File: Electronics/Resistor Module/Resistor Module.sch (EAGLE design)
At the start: 121 parts, among them U1 74HC595D, U2 74HC595D, U3 74HC595D, U4 74HC595D, U5 25AA010A

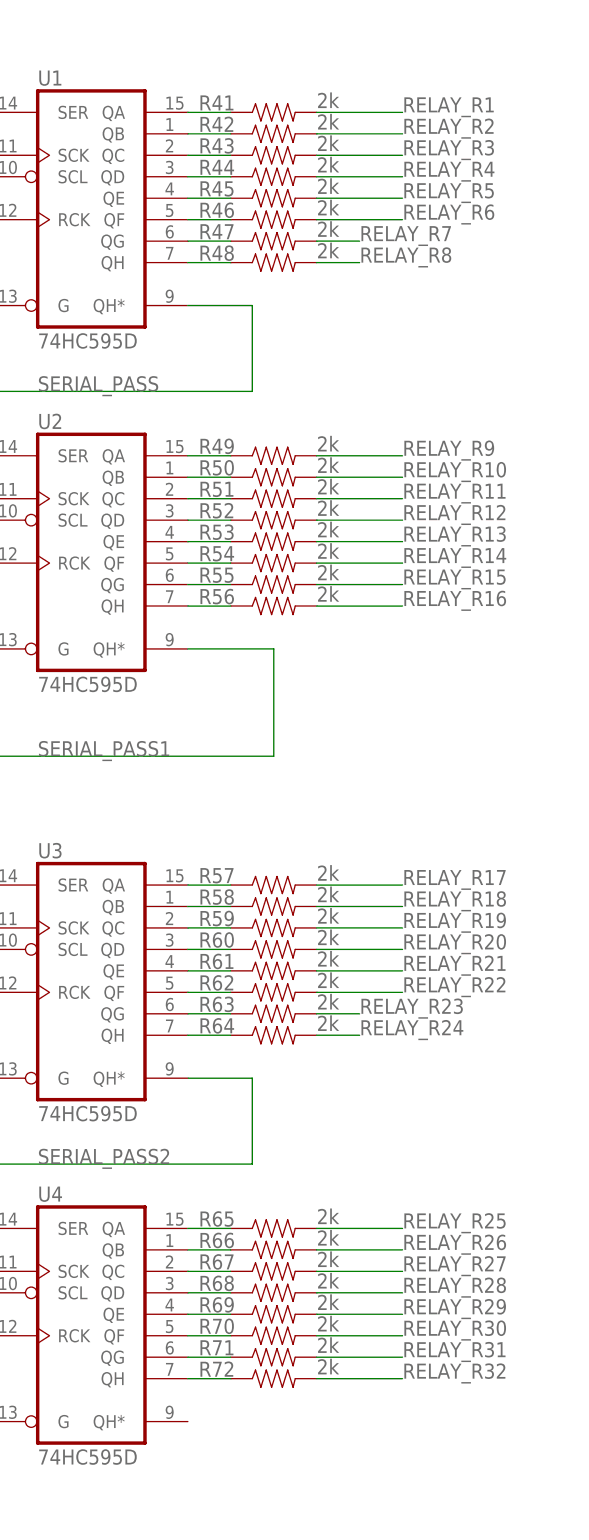
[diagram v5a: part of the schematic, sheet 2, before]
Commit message: Finished routing. Was more convenient for routing to use inverted byte order for the serial passing.
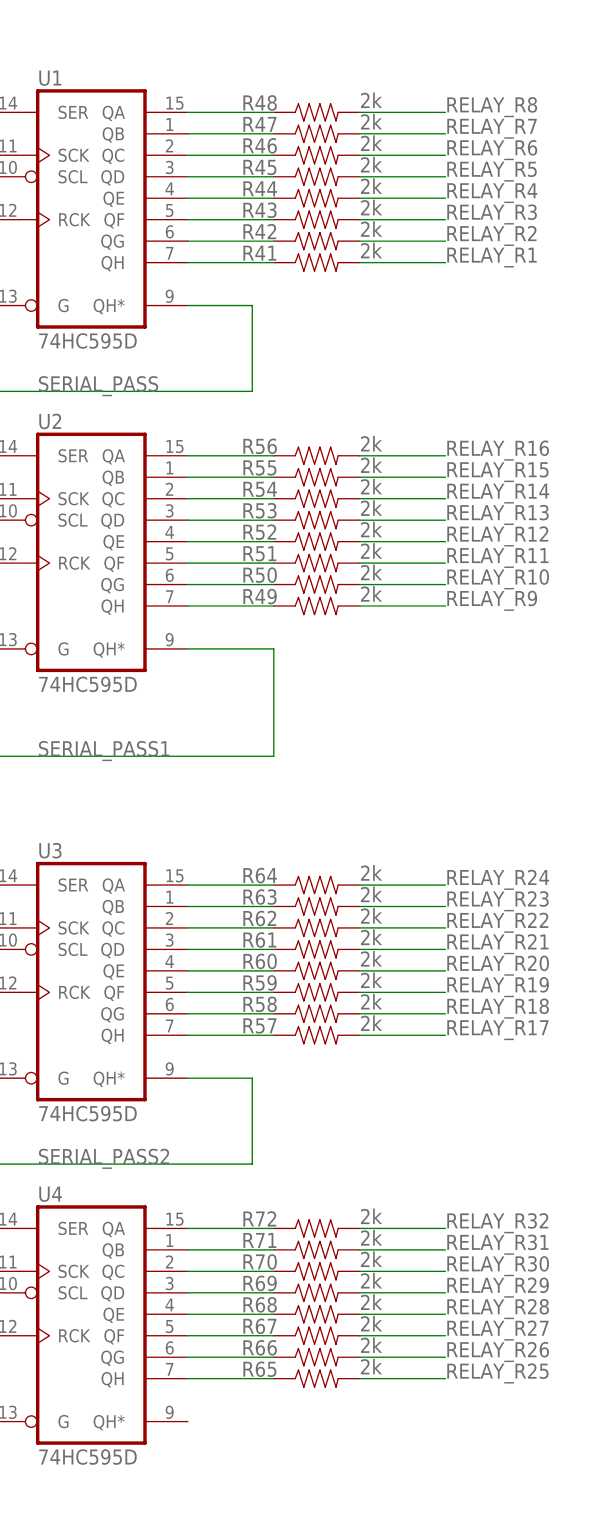
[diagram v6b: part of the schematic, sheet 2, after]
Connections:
- removed net N$61: R49.1, U2A.QA
- removed net N$62: R57.1, U3A.QA
- removed net N$64: R65.1, U4A.QA
- new net N$40: R67.1, U4A.QF
- new net N$43: R66.1, U4A.QG
- new net N$9: R46.1, U1A.QC
- net GND: no longer S17.C-, S18.C-, S19.C-, S20.C-, S21.C-, S22.C-, S23.C-, S24.C-, S25.C-, S26.C-, S27.C-, S28.C-, S29.C-, S30.C-, S31.C-, S32.C-
- net GND_2: now also S17.C-, S18.C-, S19.C-, S20.C-, S21.C-, S22.C-, S23.C-, S24.C-, S25.C-, S26.C-, S27.C-, S28.C-, S29.C-, S30.C-, S31.C-, S32.C-
- net N$1: now also U1A.QA; no longer U1A.QH
- net N$12: now also R45.1, U1A.QD; no longer R46.1, U1A.QF
- net N$13: now also R44.1; no longer R45.1
- net N$14: now also R43.1, U1A.QF; no longer R44.1, U1A.QD
- net N$16: now also R42.1, U1A.QG; no longer R43.1, U1A.QC
- net N$17: now also R41.1, U1A.QH; no longer R42.1, U1A.QB
- net N$18: now also R56.1, U2A.QA; no longer R50.1, U2A.QB
- net N$19: now also R55.1, U2A.QB; no longer R51.1, U2A.QC
- net N$2: now also U1A.QB; no longer U1A.QG
- net N$20: now also R54.1, U2A.QC; no longer R52.1, U2A.QD
- net N$21: now also U2A.QD; no longer U2A.QE
- net N$22: now also R52.1, U2A.QE; no longer R54.1, U2A.QF
- net N$23: now also R51.1, U2A.QF; no longer R55.1, U2A.QG
- net N$24: now also R50.1, U2A.QG; no longer R56.1, U2A.QH
- net N$26: now also R49.1, U2A.QH; no longer R64.1, U3A.QH
- net N$27: now also R64.1, U3A.QA; no longer R63.1, U3A.QG
- net N$28: now also R63.1, U3A.QB; no longer R62.1, U3A.QF
- net N$29: now also R62.1, U3A.QC; no longer R61.1, U3A.QE
- net N$30: now also R61.1; no longer R60.1
- net N$31: now also R60.1, U3A.QE; no longer R59.1, U3A.QC
- net N$32: now also R59.1, U3A.QF; no longer R58.1, U3A.QB
- net N$33: now also R58.1, U3A.QG; no longer R66.1, U4A.QB
- net N$34: now also R57.1, U3A.QH; no longer R67.1, U4A.QC
- net N$35: now also R72.1, U4A.QA; no longer R68.1, U4A.QD
- net N$36: now also R71.1, U4A.QB; no longer R69.1, U4A.QE
- net N$37: now also U4A.QC; no longer U4A.QF
- net N$38: now also R69.1, U4A.QD; no longer R71.1, U4A.QG
- net N$39: now also R68.1, U4A.QE; no longer R72.1, U4A.QH
- net N$57: now also R65.1, U4A.QH; no longer R41.1, U1A.QA
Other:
- moved on the sheet: R41, R42, R43, R44, R45, R46, R47, R48, R49, R50, R51, R52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

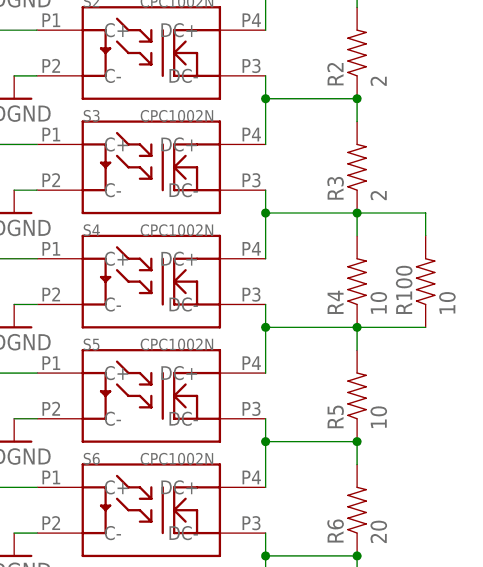
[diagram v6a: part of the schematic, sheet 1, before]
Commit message: Finished routing and silk cleanup. Ready for final review and release.
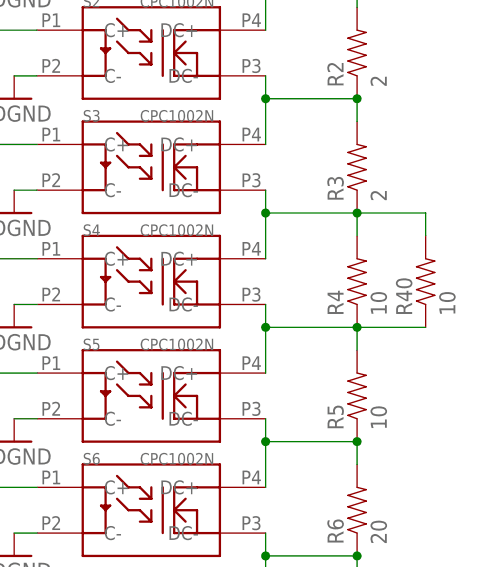
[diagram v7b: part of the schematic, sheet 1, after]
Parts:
- renumbered R100 to R40
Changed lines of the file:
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@@
 <part name="S11" library="Resistor Module Library" deviceset="CPC1002N" device=""/>
 <part name="S12" library="Resistor Module Library" deviceset="CPC1002N" device=""/>
-<part name="R100" library="Resistor Module Library" deviceset="RESISTOR" device="1206" value="10"/>
+<part name="R40" library="Resistor Module Library" deviceset="RESISTOR" device="1206" value="10"/>
 <part name="R80" library="Resistor Module Library" deviceset="RESISTOR" device="1206" value="100"/>
 <part name="R120" library="Resistor Module Library" deviceset="RESISTOR" device="1206" value="1k"/>
@@
 <attribute name="VALUE" x="-24.13" y="-134.62" size="1.27" layer="95"/>
 </instance>
-<instance part="R100" gate="G$1" x="7.62" y="-38.1" rot="R90"/>
+<instance part="R40" gate="G$1" x="7.62" y="-38.1" rot="R90"/>
 <instance part="R80" gate="G$1" x="7.62" y="-88.9" rot="R90"/>
 <instance part="R120" gate="G$1" x="7.62" y="-139.7" rot="R90"/>
@@
 <junction x="-10.16" y="-30.48"/>
 <junction x="0" y="-30.48"/>
-<pinref part="R100" gate="G$1" pin="2"/>
+<pinref part="R40" gate="G$1" pin="2"/>
 <wire x1="7.62" y1="-33.02" x2="7.62" y2="-30.48" width="0.1524" layer="91"/>
 <wire x1="7.62" y1="-30.48" x2="0" y2="-30.48" width="0.1524" layer="91"/>
@@
 <junction x="0" y="-43.18"/>
 <junction x="-10.16" y="-43.18"/>
-<pinref part="R100" gate="G$1" pin="1"/>
+<pinref part="R40" gate="G$1" pin="1"/>
 <wire x1="0" y1="-43.18" x2="7.62" y2="-43.18" width="0.1524" layer="91"/>
 </segment>
